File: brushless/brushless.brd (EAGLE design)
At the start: 30 x 48 mm, 74 parts, among them Q1 BUK7Y12-40E, Q2 BUK7Y12-40E, Q3 BUK7Y12-40E, Q4 BUK7Y12-40E, Q5 BUK7Y12-40E, Q6 BUK7Y12-40E, X2 MOTOR

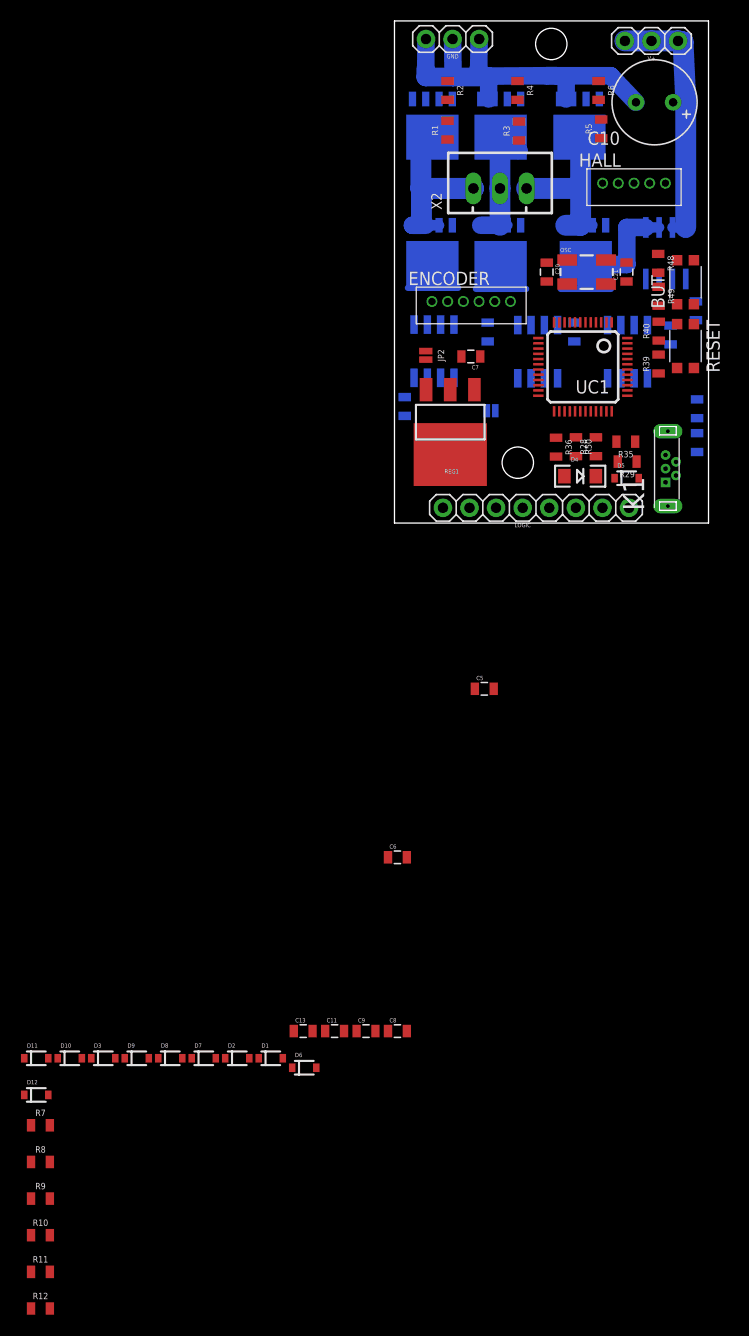
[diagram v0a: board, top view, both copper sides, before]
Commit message: brushless board rerouted
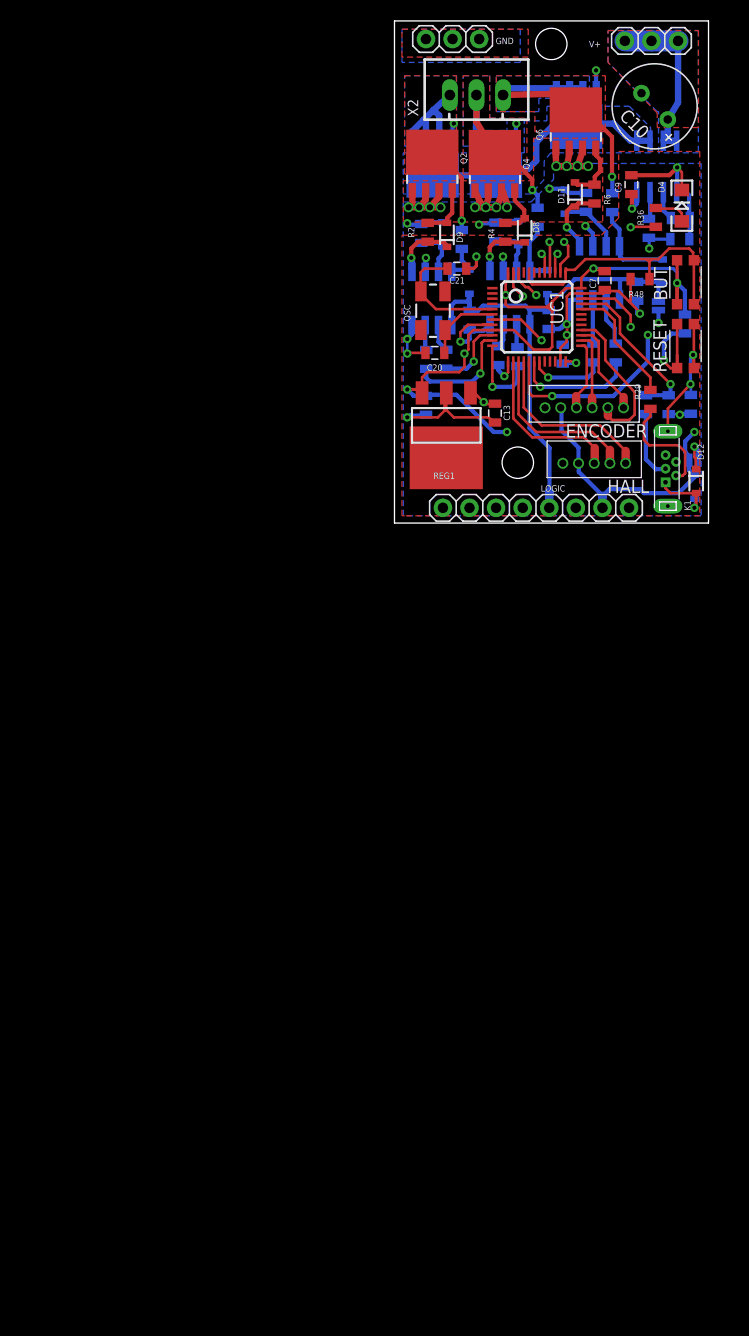
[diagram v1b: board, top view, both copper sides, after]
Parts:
- removed R39, R49: 1K, SparkFun-Resistors:0805
- moved R12 105.5 mm to (18.9, 14.3), flipped to the bottom, turned to 90 degrees
- moved R11 103.6 mm to (21.1, 14.3), flipped to the bottom, turned to 90 degrees
- moved D11 97.3 mm to (17.2, 29.4), turned to 90 degrees
- moved R10 94.7 mm to (9.85, 14.0), flipped to the bottom, turned to 90 degrees
- moved D10 94.5 mm to (16.2, 28.7), flipped to the bottom, turned to 90 degrees
- moved R9 92.4 mm to (11.7, 13.9), flipped to the bottom, turned to 90 degrees
- moved D3 92.2 mm to (25.5, 22.1), flipped to the bottom, turned to 270 degrees
- moved D12 86.1 mm to (28.7, 2.04), turned to 270 degrees
- moved D8 86.0 mm to (12.4, 26.0), turned to 90 degrees
- moved R8 85.1 mm to (2.96, 13.7), flipped to the bottom, turned to 90 degrees
- moved C9 84.7 mm to (22.6, 30.4), turned to 90 degrees
- moved D7 84.4 mm to (11.7, 25.7), flipped to the bottom, turned to 90 degrees
- moved D9 84.1 mm to (4.93, 25.6), turned to 90 degrees
- moved R7 82.8 mm to (4.87, 13.7), flipped to the bottom, turned to 90 degrees
- moved D1 80.4 mm to (4.49, 25.6), flipped to the bottom, turned to 90 degrees
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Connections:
- removed net N$1: R39.1, RESET.P$1, RESET.P$3
- removed net N$26: BUT.P$1, BUT.P$3, R49.2
- removed net VUSB1: D12.2
- net +3V3: now also BUT.P$1, BUT.P$3; no longer R49.1
- net AGND: now also RESET.P$1, RESET.P$3; no longer R39.2
- net VUSB: now also D12.2
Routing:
- net +3V3: track 0.00 -> 99.2 mm, vias 0 -> 7
- net AGND: track 38.3 -> 120.7 mm, vias 0 -> 24
- net VCC: track 0.00 -> 60.4 mm, vias 0 -> 2
- net VDRIVER: track 0.00 -> 51.8 mm
- net CS: track 0.00 -> 41.2 mm, vias 0 -> 1
- net MISO: track 0.00 -> 38.3 mm, vias 0 -> 1
- net SCK: track 0.00 -> 36.6 mm, vias 0 -> 1
- net MOSI: track 0.00 -> 35.8 mm, vias 0 -> 1
- net DISC: track 0.00 -> 30.2 mm, vias 0 -> 2
- net CUR: track 0.00 -> 29.9 mm, vias 0 -> 3
- net RESET: track 0.00 -> 29.4 mm, vias 0 -> 2
- net N$22: track 0.00 -> 29.4 mm, vias 0 -> 2
- net BUTTON: track 0.00 -> 26.8 mm
- net N$7: track 0.00 -> 21.2 mm, vias 0 -> 2
- net V_PHASE: track 13.6 -> 32.9 mm, vias 0 -> 2
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- added copper zone on layer 1, net AGND
- added copper zone on layer 15, net AGND
- added copper zone on layer 16, net AGND
- added copper zone on layer 2, net AGND
- added copper zone on layer 1, net U_PHASE
- added copper zone on layer 16, net U_PHASE
- added copper zone on layer 1, net V+
- added copper zone on layer 15, net V+
- added copper zone on layer 16, net V+
- added copper zone on layer 16, net V+_MOS
- added copper zone on layer 1, net V_PHASE
- added copper zone on layer 16, net V_PHASE
- added copper zone on layer 1, net W_PHASE
- added copper zone on layer 16, net W_PHASE

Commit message: clearence error on brushles board corrected
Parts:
- moved LOGIC 7.62 mm to (4.55, -0.51)
- moved GND 4.02 mm to (2.93, 44.3)
- moved V+ 4.02 mm to (21.9, 44.1)
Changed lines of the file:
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@@
 <setting verticaltext="up"/>
 </settings>
-<grid distance="0.127" unitdist="mm" unit="mm" style="lines" multiple="1" display="no" altdistance="0.01" altunitdist="mm" altunit="mm"/>
+<grid distance="1.27" unitdist="mm" unit="mm" style="lines" multiple="1" display="yes" altdistance="0.01" altunitdist="mm" altunit="mm"/>
 <layers>
-<layer number="1" name="Top" color="4" fill="1" visible="yes" active="yes"/>
+<layer number="1" name="Top" color="4" fill="1" visible="no" active="yes"/>
 <layer number="2" name="Route2" color="11" fill="1" visible="yes" active="yes"/>
 <layer number="3" name="Route3" color="4" fill="3" visible="no" active="no"/>
@@
 <layer number="13" name="Route13" color="4" fill="5" visible="no" active="no"/>
 <layer number="14" name="Route14" color="1" fill="6" visible="no" active="no"/>
-<layer number="15" name="Route15" color="14" fill="1" visible="yes" active="yes"/>
-<layer number="16" name="Bottom" color="1" fill="1" visible="yes" active="yes"/>
+<layer number="15" name="Route15" color="14" fill="1" visible="no" active="yes"/>
+<layer number="16" name="Bottom" color="1" fill="1" visible="no" active="yes"/>
 <layer number="17" name="Pads" color="2" fill="1" visible="yes" active="yes"/>
 <layer number="18" name="Vias" color="2" fill="1" visible="yes" active="yes"/>
@@
 <attribute name="VALUE" x="5.9481" y="7.5565" size="0.4064" layer="27" rot="R180"/>
 </element>
-<element name="V+" library="rhoban" package="CONNEC_1X03" value="CONNEC_1X03" x="25.74" y="45.363" locked="yes" smashed="yes" rot="R180">
-<attribute name="FARNELL" value="1022248" x="25.74" y="45.363" size="1.778" layer="27" rot="R180" display="off"/>
-<attribute name="NAME" x="19.644" y="44.093" size="0.6096" layer="25" ratio="10" rot="R180"/>
-</element>
-<element name="GND" library="rhoban" package="CONNEC_1X03" value="CONNEC_1X03" x="6.74" y="45.54" locked="yes" smashed="yes" rot="R180">
-<attribute name="FARNELL" value="1022248" x="6.74" y="45.54" size="1.778" layer="27" rot="R180" display="off"/>
-<attribute name="NAME" x="11.312" y="44.397" size="0.6096" layer="25" ratio="10" rot="R180"/>
-</element>
-<element name="LOGIC" library="rhoban" package="CONNEC_1X08" value="CONNEC_1X08" x="12.1672" y="-0.5128" locked="yes" smashed="yes" rot="R180">
-<attribute name="FARNELL" value="1022256" x="12.1672" y="-0.5128" size="1.778" layer="27" rot="R180" display="off"/>
-<attribute name="NAME" x="16.2312" y="1.6462" size="0.6096" layer="25" ratio="10" rot="R180"/>
+<element name="V+" library="rhoban" package="CONNEC_1X03" value="CONNEC_1X03" x="21.93" y="44.093" smashed="yes" rot="R180">
+<attribute name="FARNELL" value="1022248" x="21.93" y="44.093" size="1.778" layer="27" rot="R180" display="off"/>
+<attribute name="NAME" x="15.834" y="42.823" size="0.6096" layer="25" ratio="10" rot="R180"/>
+</element>
+<element name="GND" library="rhoban" package="CONNEC_1X03" value="CONNEC_1X03" x="2.93" y="44.27" smashed="yes" rot="R180">
+<attribute name="FARNELL" value="1022248" x="2.93" y="44.27" size="1.778" layer="27" rot="R180" display="off"/>
+<attribute name="NAME" x="7.502" y="43.127" size="0.6096" layer="25" ratio="10" rot="R180"/>
+</element>
+<element name="LOGIC" library="rhoban" package="CONNEC_1X08" value="CONNEC_1X08" x="4.5472" y="-0.5128" smashed="yes" rot="R180">
+<attribute name="FARNELL" value="1022256" x="4.5472" y="-0.5128" size="1.778" layer="27" rot="R180" display="off"/>
+<attribute name="NAME" x="8.6112" y="1.6462" size="0.6096" layer="25" ratio="10" rot="R180"/>
 </element>
 <element name="Q1" library="transistor-power" package="SOT669" value="BUK7Y12-40E" x="3.56" y="32.269" smashed="yes" rot="MR180">
